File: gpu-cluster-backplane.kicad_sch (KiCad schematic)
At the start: 2 parts

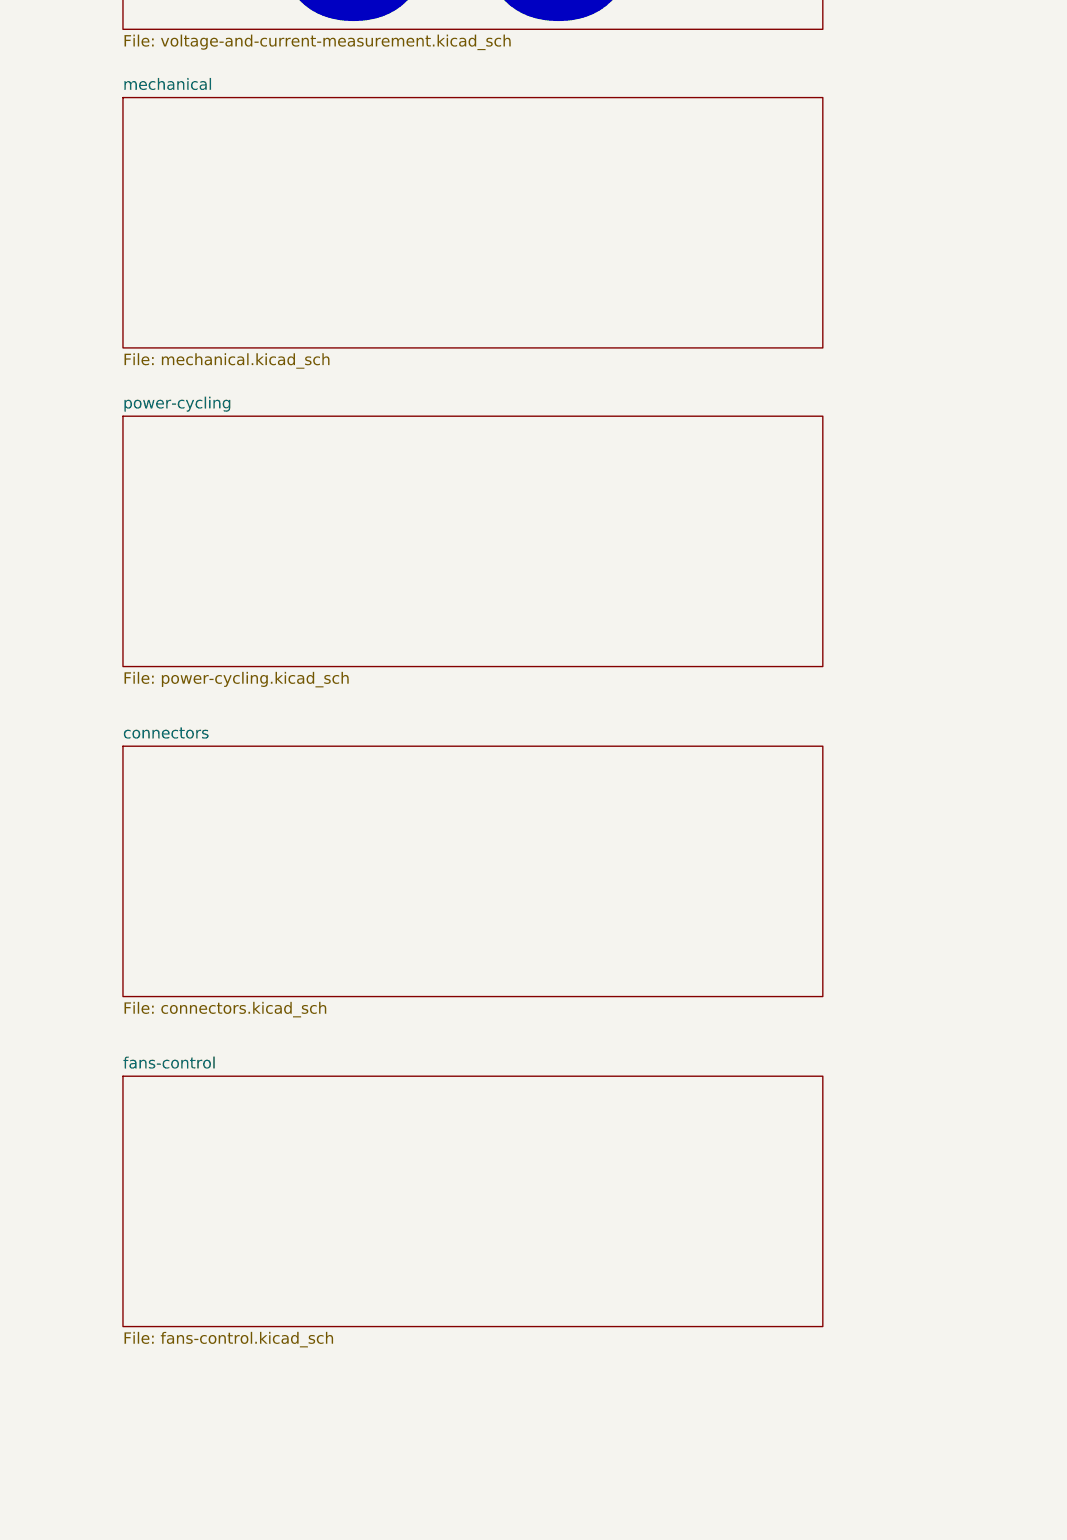
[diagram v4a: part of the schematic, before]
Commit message: Updated sch power cycling section
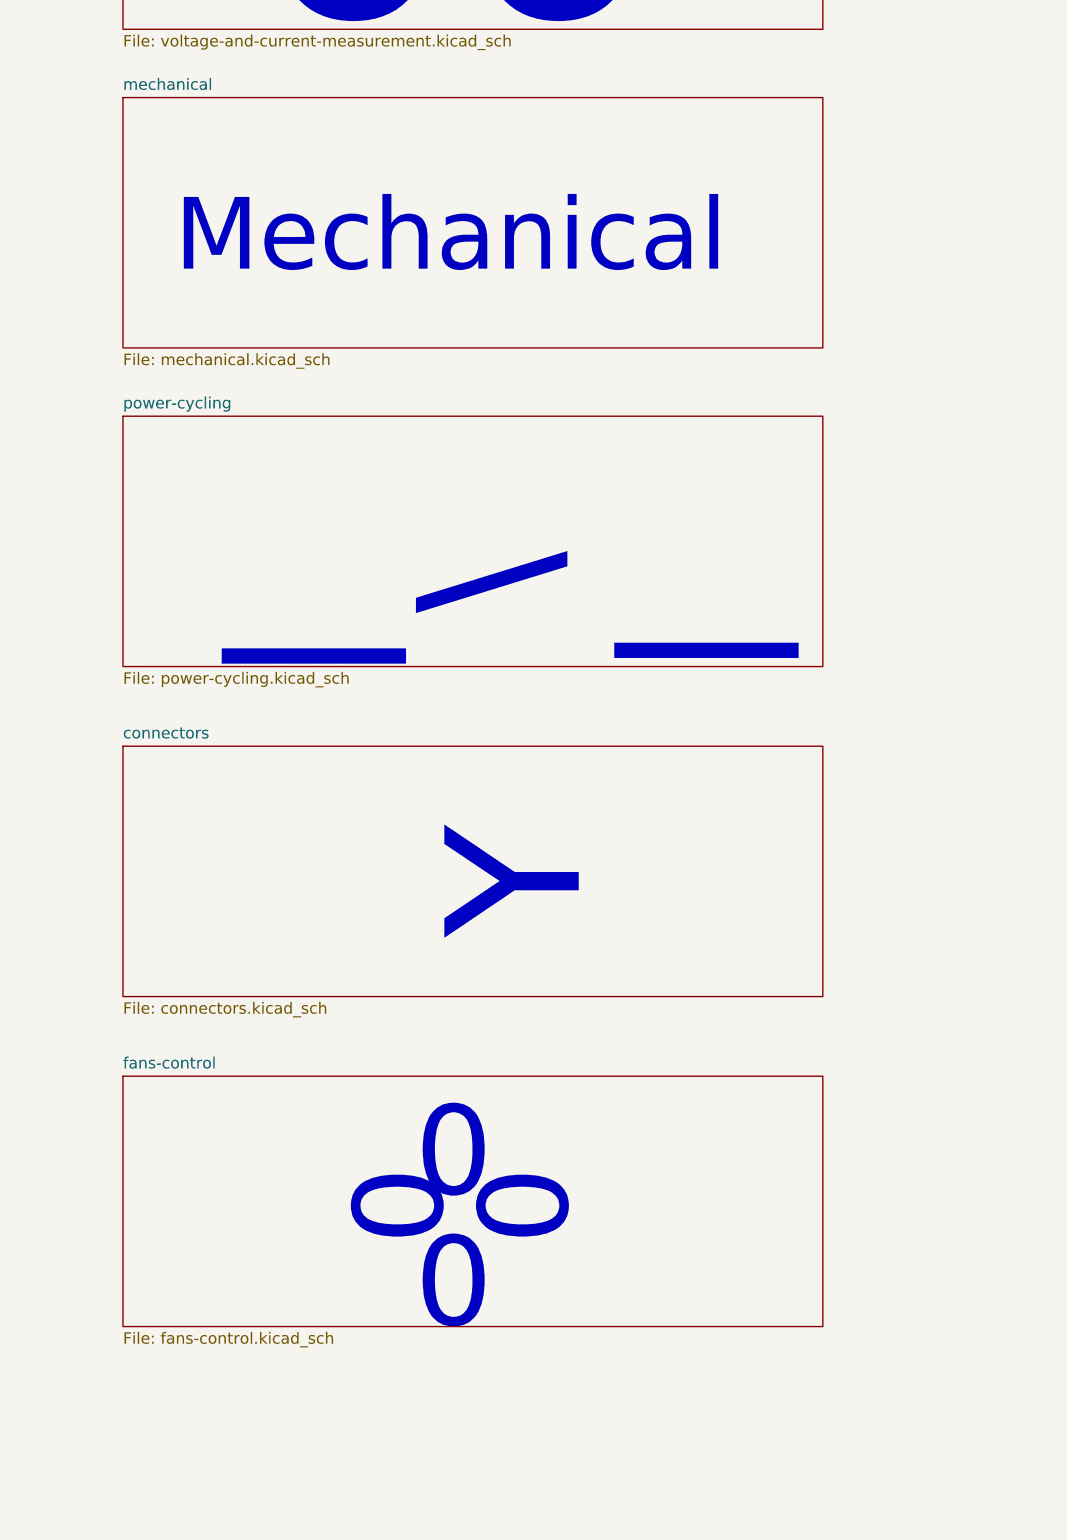
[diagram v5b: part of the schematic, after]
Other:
- note added: "0"
- note added: "Mechanical"
- note added: "Y"
- note added: "\"
- note added: "|"

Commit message: WIP Standarization
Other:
- removed sheet Power Cycling & Current Measurement
